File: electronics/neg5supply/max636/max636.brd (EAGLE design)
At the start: 24.9 x 21.6 mm, 14 parts, among them J1 +V, J2 -V, J3 GND, J4 GND, U1 MAX636

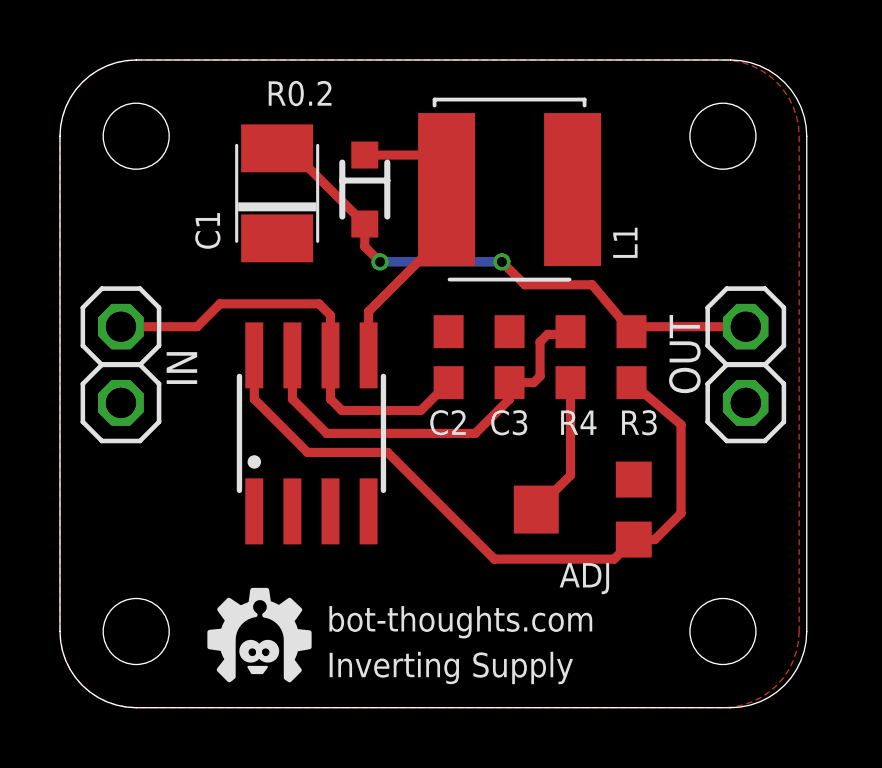
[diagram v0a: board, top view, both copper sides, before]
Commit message: changed board dimensions, revised layout
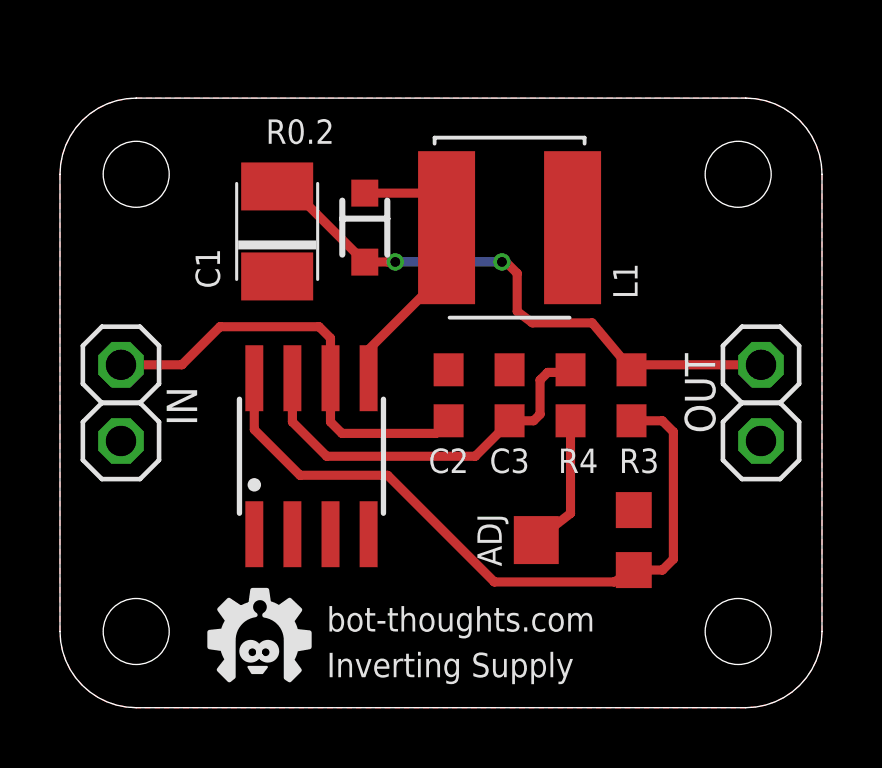
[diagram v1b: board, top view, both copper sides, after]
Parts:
- moved J2 1.37 mm to (23.4, 11.4)
- moved J3 1.37 mm to (23.4, 8.89)
- moved C1 1.27 mm to (7.24, 15.9)
- moved C2 1.27 mm to (13.0, 10.4)
- moved C3 1.27 mm to (15.0, 10.4)
- moved D1 1.27 mm to (10.2, 16.0)
- moved J1 1.27 mm to (2.03, 11.4)
- moved J4 1.27 mm to (2.03, 8.89)
- moved L1 1.27 mm to (15.0, 16.0)
- moved R3 1.27 mm to (19.1, 10.4)
- moved R4 1.27 mm to (17.0, 10.4)
- moved ADJ 1.02 mm to (17.5, 5.59)
- moved U1 0.76 mm to (8.38, 8.38)
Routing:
- net N$3: track 18.7 -> 19.5 mm
- net N$6: track 13.6 -> 13.1 mm
- net N$1: track 10.2 -> 9.65 mm
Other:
- board size 24.9 x 21.6 mm -> 25.4 x 20.3 mm
